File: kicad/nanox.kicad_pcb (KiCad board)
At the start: 4 copper layers, 61.7 x 15.9 mm, 137 parts, among them P1 likely an ESD protection diod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, P2 likely an ESD protection diod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, P3 likely an ESD protection diod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, P4 likely an ESD protection diod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, P5 likely an ESD protection diod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, SW1 push button, left, SW2 push button, right, X1 ?, X10 TI TLV61046A boost converter 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, X2 unknown, marked 2GC, X3 unknown, marked 6, X4 ?, X5 ?, X6 ?, X7 ?, X8 ?, X9 NXP PMBZ5246B 16 V Zener diod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, Y1 crystal, likely the 32 MHz HSE

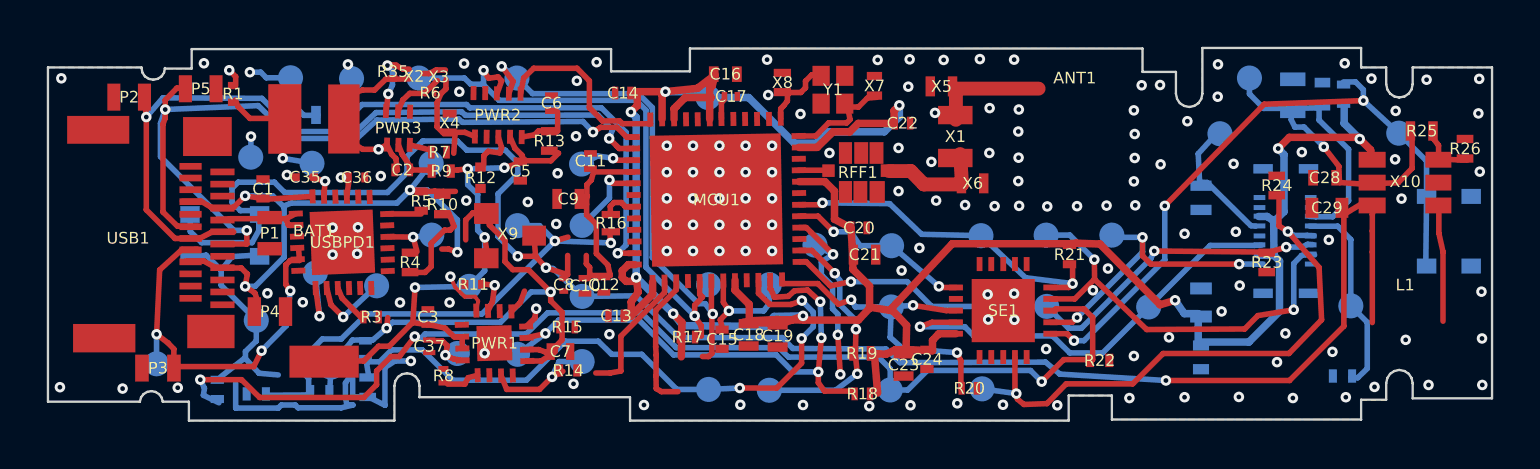
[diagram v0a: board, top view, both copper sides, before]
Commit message: Add X11, the 4-pad part marked AF between C9 and C8/C10
Three traces ended on it unconnected: the supply on the left button
(pad 19), VDDUSB (the MCU's USB supply, with C9-C12) and the net from MCU
PB3 and the charger input through R16/R29. Its fourth pad is ground,
joined to C10's ground pad, and carries the dot seen on the part. From
those nets it is likely a small LDO making VDDUSB, enabled by the MCU or
by USB power; not confirmed.

Co-Authored-By: Claude Opus 5.5 <noreply@anthropic.com>
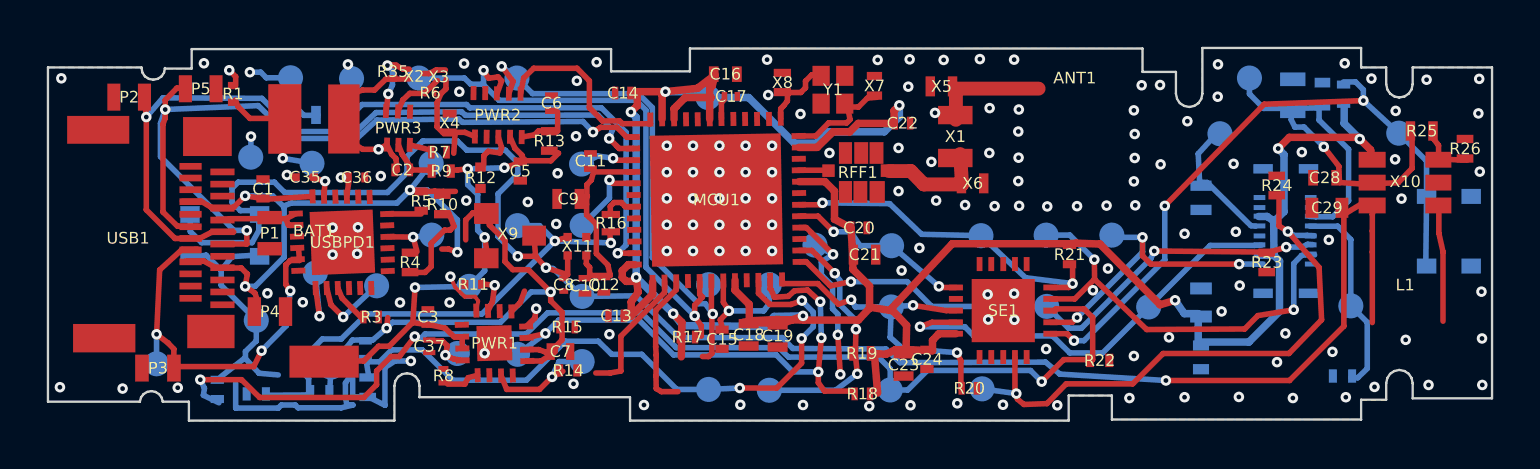
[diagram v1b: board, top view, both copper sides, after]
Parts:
- added X11: unknown, marked AF, likely a small LDO regulator, , F.Cu at (23.8, 19.7)
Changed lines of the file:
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@@
+	(footprint ""
+		(layer "F.Cu")
+		(at 23.809523 19.738095)
+		(descr "4 pads, ~1.2 mm square; Small square part with a pad at each corner, between C9 and C8/C10. Pads named by corner in the front photo. Likely roles from its nets: TL input from the supply on the left button (pad 19), TR output to VDDUSB (the MCU's USB supply, pin 40, with C9-C12), BL enable from MCU PB3 (through R16) and the charger input (through R29), BR GND, which also goes to C10's ground pad and carries the dot seen on the part; not confirmed")
+		(property "Reference" "X11"
+			(at 0 0 0)
+			(layer "F.SilkS")
+			(effects
+				(font
+					(size 0.5 0.5)
+					(thickness 0.08)
+				)
+			)
+		)
+		(property "Value" "unknown, marked AF, likely a small LDO regulator"
+			(at 0 0 0)
+			(layer "F.Fab")
+			(hide yes)
+			(effects
+				(font
+					(size 1.27 1.27)
+				)
+			)
+		)
+		(property "Datasheet" ""
+			(at 0 0 0)
+			(layer "F.Fab")
+			(hide yes)
+			(effects
+				(font
+					(size 1.27 1.27)
+				)
+			)
+		)
+		(property "Description" ""
+			(at 0 0 0)
+			(layer "F.Fab")
+			(hide yes)
+			(effects
+				(font
+					(size 1.27 1.27)
+				)
+			)
+		)
+		(duplicate_pad_numbers_are_jumpers no)
+		(fp_line
+			(start -0.595238 -0.595238)
+			(end -0.595238 0.595238)
+			(stroke
+				(width 0.08)
+				(type default)
+			)
+			(layer "F.Fab")
+		)
+		(fp_line
+			(start -0.595238 0.595238)
+			(end 0.595238 0.595238)
+			(stroke
+				(width 0.08)
+				(type default)
+			)
+			(layer "F.Fab")
+		)
+		(fp_line
+			(start 0.595238 -0.595238)
+			(end -0.595238 -0.595238)
+			(stroke
+				(width 0.08)
+				(type default)
+			)
+			(layer "F.Fab")
+		)
+		(fp_line
+			(start 0.595238 0.595238)
+			(end 0.595238 -0.595238)
+			(stroke
+				(width 0.08)
+				(type default)
+			)
+			(layer "F.Fab")
+		)
+		(pad "BL" smd rect
+			(at -0.404762 -0.392857)
+			(size 0.357142 0.357142)
+			(layers "F.Cu" "F.Mask" "F.Paste")
+			(net "Net-T40")
+			(thermal_bridge_angle 45)
+		)
+		(pad "BR" smd rect
+			(at 0.392857 -0.392857)
+			(size 0.357142 0.357142)
+			(layers "F.Cu" "F.Mask" "F.Paste")
+			(net "GND")
+			(thermal_bridge_angle 45)
+		)
+		(pad "TL" smd rect
+			(at -0.404762 0.392857)
+			(size 0.357142 0.357142)
+			(layers "F.Cu" "F.Mask" "F.Paste")
+			(net "Left button power (pad 19)")
+			(thermal_bridge_angle 45)
+		)
+		(pad "TR" smd rect
+			(at 0.392857 0.392857)
+			(size 0.357142 0.357142)
+			(layers "F.Cu" "F.Mask" "F.Paste")
+			(net "VDDUSB")
+			(thermal_bridge_angle 45)
+		)
+		(embedded_fonts no)
+		(model "/home/magicaltux/projects/ledger_nano_x_pads/kicad/3d/X11.wrl"
+			(offset
+				(xyz 0 0 0)
+			)
+			(scale
+				(xyz 1 1 1)
+			)
+			(rotate
+				(xyz 0 0 0)
+			)
+		)
+	)
 	(footprint ""
 		(layer "F.Cu")

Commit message: Add X12, the likely USB power switch across from X9
A black 3-terminal part with no pads drawn. VBUS and the charger input
already ended on two of its pads, and the net through R10 (from VBUS) and
R4 (from the STUSB4500L's VBUS_EN_SNK) passes over the third: the classic
P-MOSFET sink switch, source on VBUS, drain on the charger input, gate
held off by R10 until the USB-PD controller pulls it low. The gate net is
named, and the charger input and VBUS_EN_SNK descriptions point to it.

Co-Authored-By: Claude Opus 5.5 <noreply@anthropic.com>
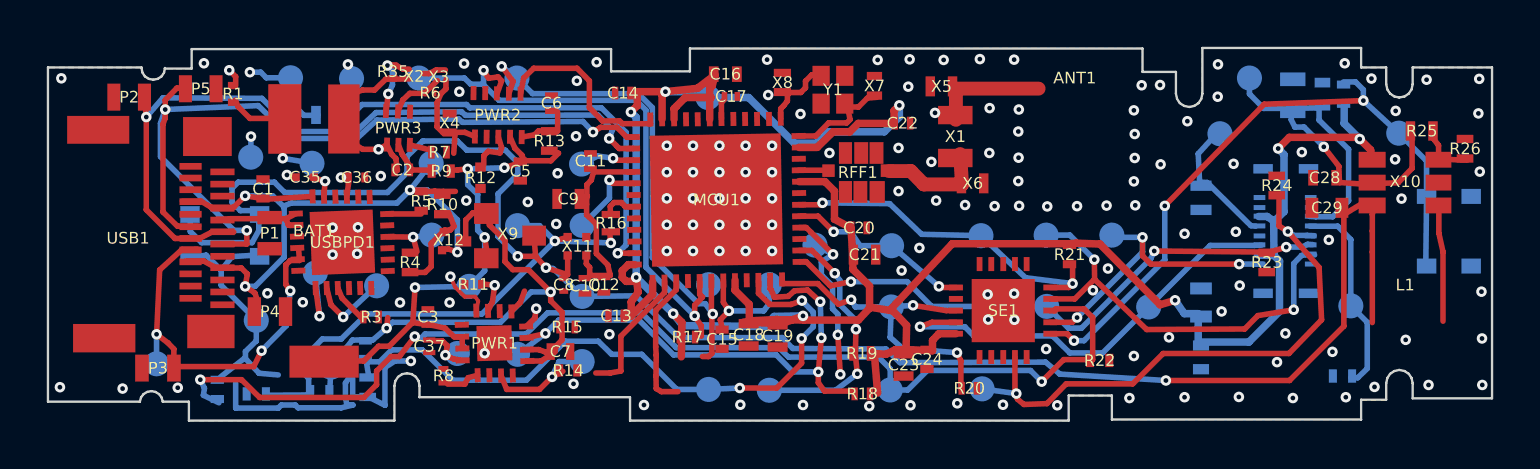
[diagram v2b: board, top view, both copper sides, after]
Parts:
- added X12: unknown, likely a P-channel MOSFET: the USB power switch, , F.Cu at (18.3, 19.5)
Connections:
- net Net-T75 renamed USB power switch gate?

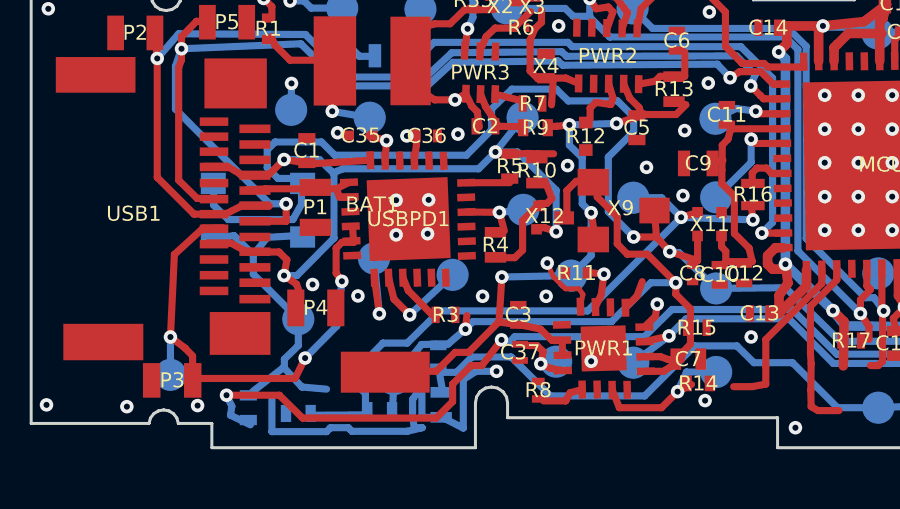
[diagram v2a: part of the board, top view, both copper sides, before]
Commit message: Size R3 to the real part so it joins PD DISCH to the charger input
R3 was drawn too small: the real resistor spans x 1216-1338 in the bare
photo, and its right pad is where the charger-input trace stub ends. It
now connects the STUSB4500L's DISCH pin to the charger input, its usual
discharge resistor.

Co-Authored-By: Claude Opus 5.5 <noreply@anthropic.com>
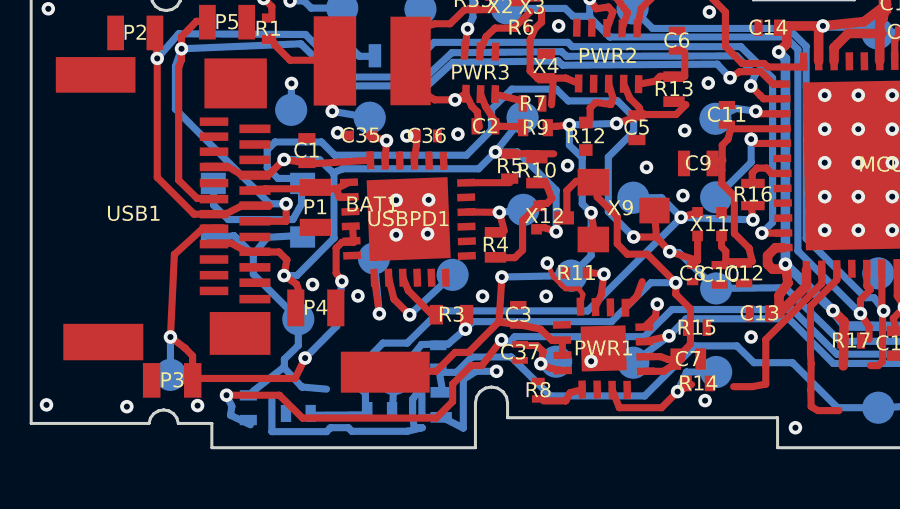
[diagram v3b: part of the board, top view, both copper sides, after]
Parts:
- moved R3 0.20 mm to (15.2, 22.8)
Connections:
- R3 pad 2: (no net) -> Charger input?
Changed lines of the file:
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@@
+	(footprint ""
+		(layer "F.Cu")
+		(at 15.20238 22.755952)
+		(descr "two-terminal SMD")
+		(property "Reference" "R3"
+			(at 0 0 0)
+			(layer "F.SilkS")
+			(effects
+				(font
+					(size 0.5 0.5)
+					(thickness 0.08)
+				)
+			)
+		)
+		(property "Value" "R"
+			(at 0 0 0)
+			(layer "F.Fab")
+			(hide yes)
+			(effects
+				(font
+					(size 1.27 1.27)
+				)
+			)
+		)
+		(property "Datasheet" ""
+			(at 0 0 0)
+			(layer "F.Fab")
+			(hide yes)
+			(effects
+				(font
+					(size 1.27 1.27)
+				)
+			)
+		)
+		(property "Description" ""
+			(at 0 0 0)
+			(layer "F.Fab")
+			(hide yes)
+			(effects
+				(font
+					(size 1.27 1.27)
+				)
+			)
+		)
+		(duplicate_pad_numbers_are_jumpers no)
+		(fp_line
+			(start -0.72619 -0.327381)
+			(end -0.72619 0.327381)
+			(stroke
+				(width 0.08)
+				(type default)
+			)
+			(layer "F.Fab")
+		)
+		(fp_line
+			(start -0.72619 0.327381)
+			(end 0.726191 0.327381)
+			(stroke
+				(width 0.08)
+				(type default)
+			)
+			(layer "F.Fab")
+		)
+		(fp_line
+			(start 0.726191 -0.327381)
+			(end -0.72619 -0.327381)
+			(stroke
+				(width 0.08)
+				(type default)
+			)
+			(layer "F.Fab")
+		)
+		(fp_line
+			(start 0.726191 0.327381)
+			(end 0.726191 -0.327381)
+			(stroke
+				(width 0.08)
+				(type default)
+			)
+			(layer "F.Fab")
+		)
+		(pad "1" smd rect
+			(at -0.505952 0)
+			(size 0.440476 0.654761)
+			(layers "F.Cu" "F.Mask" "F.Paste")
+			(net "PD DISCH")
+			(thermal_bridge_angle 45)
+		)
+		(pad "2" smd rect
+			(at 0.505953 0)
+			(size 0.440476 0.654761)
+			(layers "F.Cu" "F.Mask" "F.Paste")
+			(net "Charger input?")
+			(thermal_bridge_angle 45)
+		)
+		(embedded_fonts no)
+		(model "/usr/share/kicad/3dmodels/Resistor_SMD.3dshapes/R_0603_1608Metric.step"
+			(offset
+				(xyz 0 0 0)
+			)
+			(scale
+				(xyz 1 1 1)
+			)
+			(rotate
+				(xyz 0 0 0)
+			)
+		)
+	)
 	(footprint ""
 		(layer "F.Cu")
@@
 			)
 		)
-	)
-	(footprint ""
-		(layer "F.Cu")
-		(at 15 22.761904)
-		(descr "two-terminal SMD")
-		(property "Reference" "R3"
-			(at 0 0 0)
-			(layer "F.SilkS")
-			(effects
-				(font
-					(size 0.5 0.5)
-					(thickness 0.08)
-				)
-			)
-		)
-		(property "Value" "R"
-			(at 0 0 0)
-			(layer "F.Fab")
-			(hide yes)
-			(effects
-				(font
-					(size 1.27 1.27)
-				)
-			)
-		)
-		(property "Datasheet" ""
-			(at 0 0 0)
-			(layer "F.Fab")
-			(hide yes)
-			(effects
-				(font
-					(size 1.27 1.27)
-				)
-			)
-		)
-		(property "Description" ""
-			(at 0 0 0)
-			(layer "F.Fab")
-			(hide yes)
-			(effects
-				(font
-					(size 1.27 1.27)
-				)
-			)
-		)
-		(duplicate_pad_numbers_are_jumpers no)
-		(fp_line
-			(start -0.464286 -0.273809)
-			(end -0.464286 0.27381)
-			(stroke
-				(width 0.08)
-				(type default)
-			)
-			(layer "F.Fab")
-		)
-		(fp_line
-			(start -0.464286 0.27381)
-			(end 0.464285 0.27381)
-			(stroke
-				(width 0.08)
-				(type default)
-			)
-			(layer "F.Fab")
-		)
-		(fp_line
-			(start 0.464285 -0.273809)
-			(end -0.464286 -0.273809)
-			(stroke
-				(width 0.08)
-				(type default)
-			)
-			(layer "F.Fab")
-		)
-		(fp_line
-			(start 0.464285 0.27381)
-			(end 0.464285 -0.273809)
-			(stroke
-				(width 0.08)
-				(type default)
-			)
-			(layer "F.Fab")
-		)
-		(pad "1" smd rect
-			(at -0.327381 0)
-			(size 0.273809 0.547619)
-			(layers "F.Cu" "F.Mask" "F.Paste")
-			(net "PD DISCH")
-			(thermal_bridge_angle 45)
-		)
-		(pad "2" smd rect
-			(at 0.32738 0)
-			(size 0.273809 0.547619)
-			(layers "F.Cu" "F.Mask" "F.Paste")
-			(thermal_bridge_angle 45)
-		)
-		(embedded_fonts no)
-		(model "/usr/share/kicad/3dmodels/Resistor_SMD.3dshapes/R_0402_1005Metric.step"
-			(offset
-				(xyz 0 0 0)
-			)
-			(scale
-				(xyz 1 1 1)
-			)
-			(rotate
-				(xyz 0 0 0)
-			)
-		)

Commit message: Identify PWR3 as a TI BQ29729 battery protection IC
Its 3T marking is TI's marking for the BQ29729 (WSON-6, 1.5 x 1.5 mm),
and its pinout matches every traced connection with our pin 1: NC (1),
COUT (2) through R6, DOUT (3) with R35 to VSS, VSS (4) on battery pad 2,
BAT (5) fed through R9 with C2, V- (6) through R7. Battery pad 2 is the
cell's negative terminal; the system ground sits beyond the protection
FETs, which are not traced yet. Pins and nets are named after it.
Connectivity is unchanged.

Co-Authored-By: Claude Opus 5.5 <noreply@anthropic.com>
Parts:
- PWR3: value unknown -> TI BQ29729 Li-ion battery protection IC (marked 3T)
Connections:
- net Net-T42 renamed Battery cell -
- net Net-T45 renamed Protection DOUT
- net Net-T46 renamed Protection COUT
- net Net-T72 renamed Protection BAT
- net Net-T73 renamed Protection V-

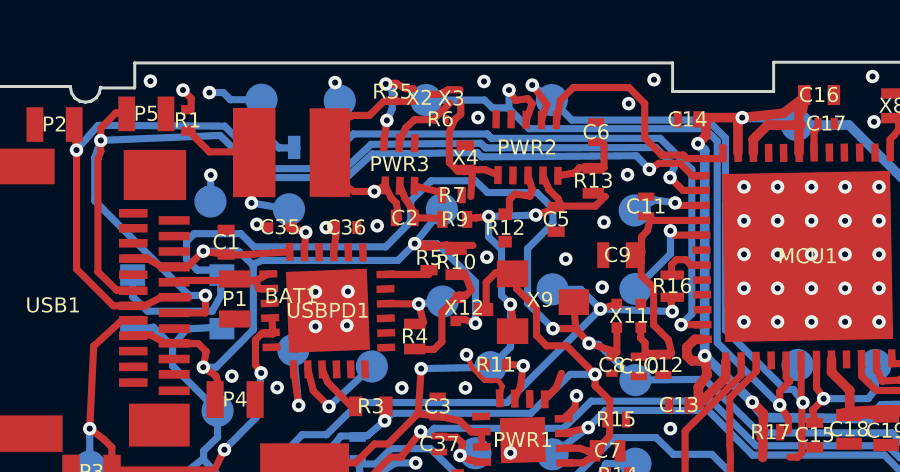
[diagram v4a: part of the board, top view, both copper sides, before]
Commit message: Size R6 and R7 to the real parts, ground X4 pad 2, name pack -
R6 and R7 were drawn too small and missed the trace between them; at their
real size R6 runs from the protection IC's COUT and R7 from its V- to the
same net, which also reaches PWR2 pin 6 and X4. With X4's other pad on GND,
that net is likely pack -, X4 the battery current-sense resistor and PWR2
a fuel gauge; descriptions say so, unconfirmed.

Co-Authored-By: Claude Opus 5.5 <noreply@anthropic.com>
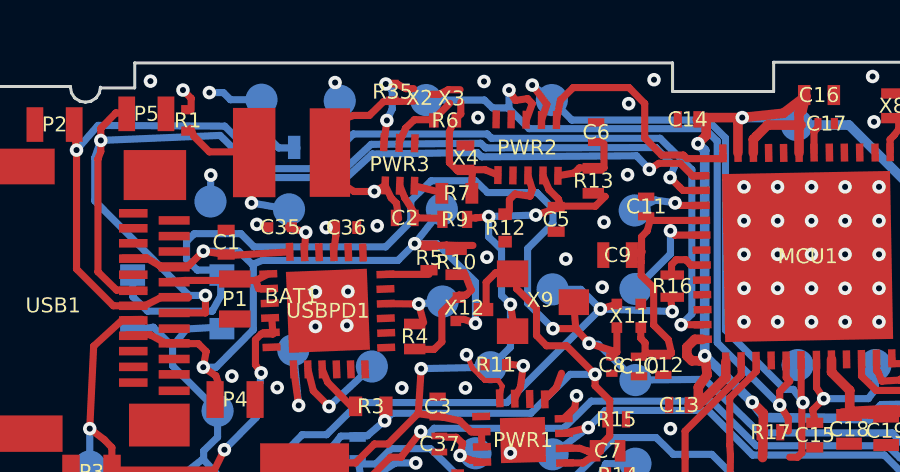
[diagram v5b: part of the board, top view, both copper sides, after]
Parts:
- moved R7 0.18 mm to (18.1, 15.7)
- moved R6 0.16 mm to (17.7, 13.2)
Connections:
- PWR2 pad 6: Net-T47 -> Pack -?
- R6 pad 2: (no net) -> Pack -?
- R7 pad 2: (no net) -> Pack -?
- X4 pad 1: Net-T47 -> Pack -?
- X4 pad 2: (no net) -> GND
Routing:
- net Pack -?: track 0.00 -> 4.80 mm
- net Net-T47: track 4.80 -> 0.00 mm

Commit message: Give X2 and X3 their pins: the battery protection FET pair
X2 and X3 were drawn as bare bodies, so the traces ending on them joined
nothing. With pads they form the BQ29729's back-to-back N-MOSFET pair:
X2 (2GC), the discharge FET, gate on DOUT and source on the battery cell -;
X3 (6), the charge FET, gate on COUT and source on pack -; their drains
joined (named Protection FET drains). Notes that called the FETs untraced
are updated. Exact parts unknown.

Co-Authored-By: Claude Opus 5.5 <noreply@anthropic.com>
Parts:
- X2: value unknown, marked 2GC -> likely an N-channel MOSFET: the battery discharge FET (marked 2GC)
- X3: value unknown, marked 6 -> likely an N-channel MOSFET: the battery charge FET (marked 6)
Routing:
- net Protection FET drains: track 0.00 -> 0.99 mm
- net Net-T63: track 0.99 -> 0.00 mm

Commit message: Confirm the battery pads: 1 temperature sensor, 2 -, 3 +
Battery pad roles are now confirmed, so the pads are named NTC, - and +,
test pads 06 and 14 lose their question marks, battery + gets a net name,
and specimen B's leg tabs say which terminal they are on.

Co-Authored-By: Claude Opus 5.5 <noreply@anthropic.com>
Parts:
- TP06: value BAT NTC? -> BAT NTC
- TP14: value VBAT? -> VBAT
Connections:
- net Battery NTC? renamed Battery NTC
- net Net-T41 renamed Battery +
